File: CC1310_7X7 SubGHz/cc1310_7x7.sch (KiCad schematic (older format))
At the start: 41 parts, among them Y1 32.768kHz

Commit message: added LEDs and buttons
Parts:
- removed L15: TBD, symbol INDUCTOR
- removed L? (x2): INDUCTOR, symbol INDUCTOR
- removed R12: DNM, symbol R
- removed R13: 0, symbol R
- added C?: 15nF, symbol C
- added C?: DNM, symbol C
- added D? (x4): LED, symbol LED
- added R? (x4): 680E, symbol R
- added R?: 1K, symbol R
- added R?: R, symbol R
- added SW? (x2): SW_PUSH, symbol SW_PUSH
- L12, L21: renamed from L?; value INDUCTOR -> 7.5nH
- Y2: renamed from Y?; value Crystal -> 24MHz
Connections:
- net labels added: DIO_19, DIO_20, DIO_21, DIO_22, DIO_23, DIO_24, DIO_25, DIO_26, DIO_27, DIO_28, DIO_29, DIO_30, JTAG_TCK, JTAG_TMS, nRESET
- net labels removed: VDD
- wire segments 60 -> 140
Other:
- moved on the sheet: C11, C21, C22, C231, C351, C41, C461, C471, C51, L11, L12, L21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

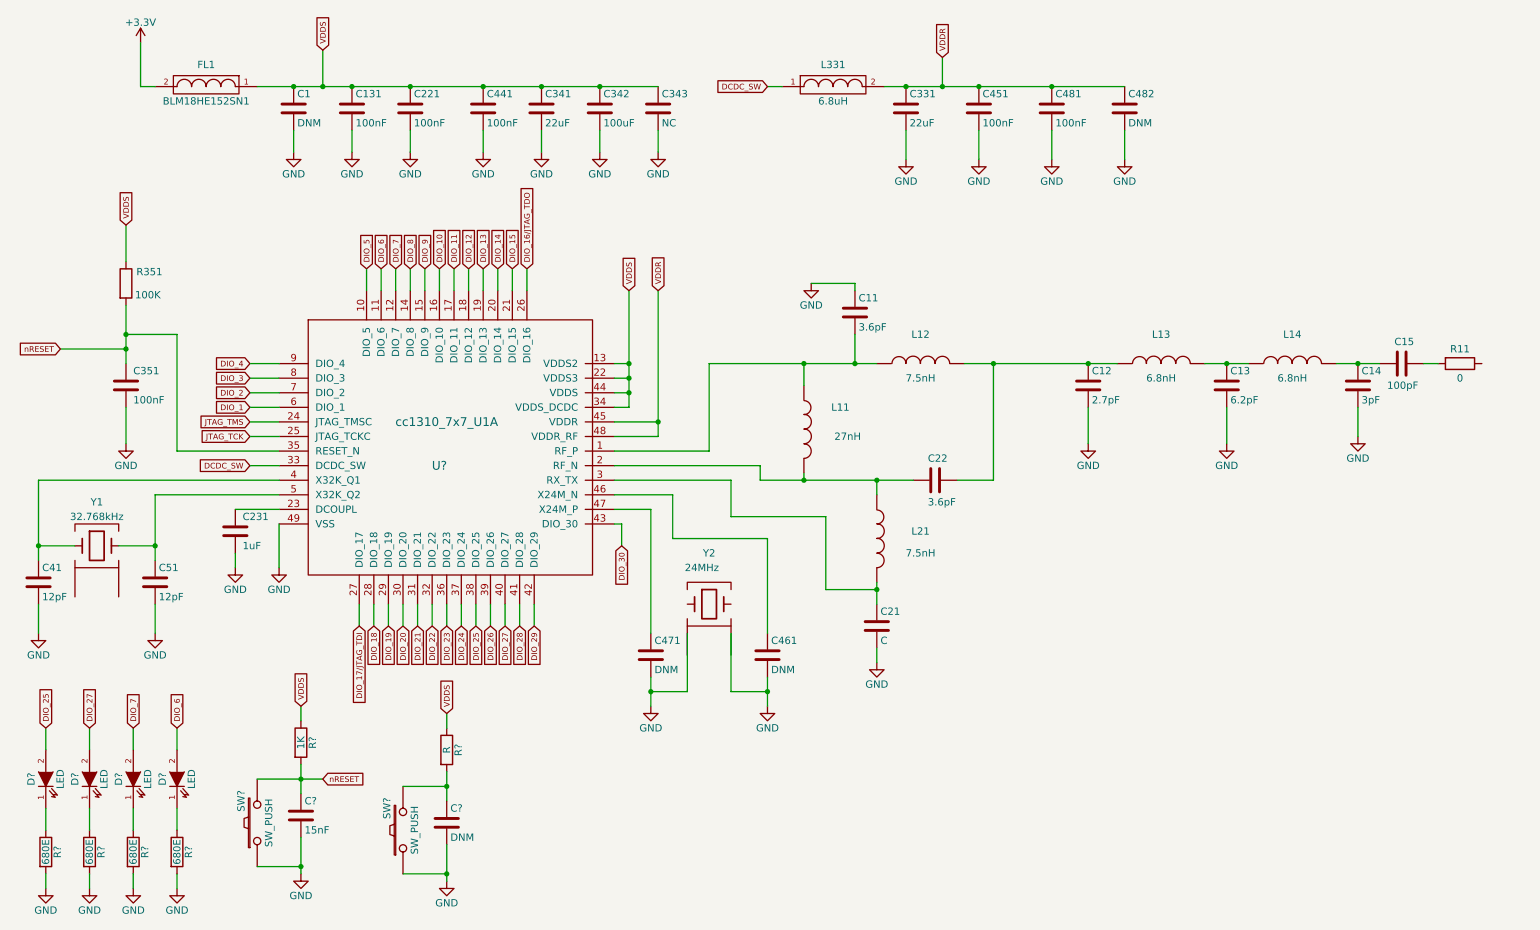
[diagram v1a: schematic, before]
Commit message: de annotated the components; added text for power section; added text for peripherals
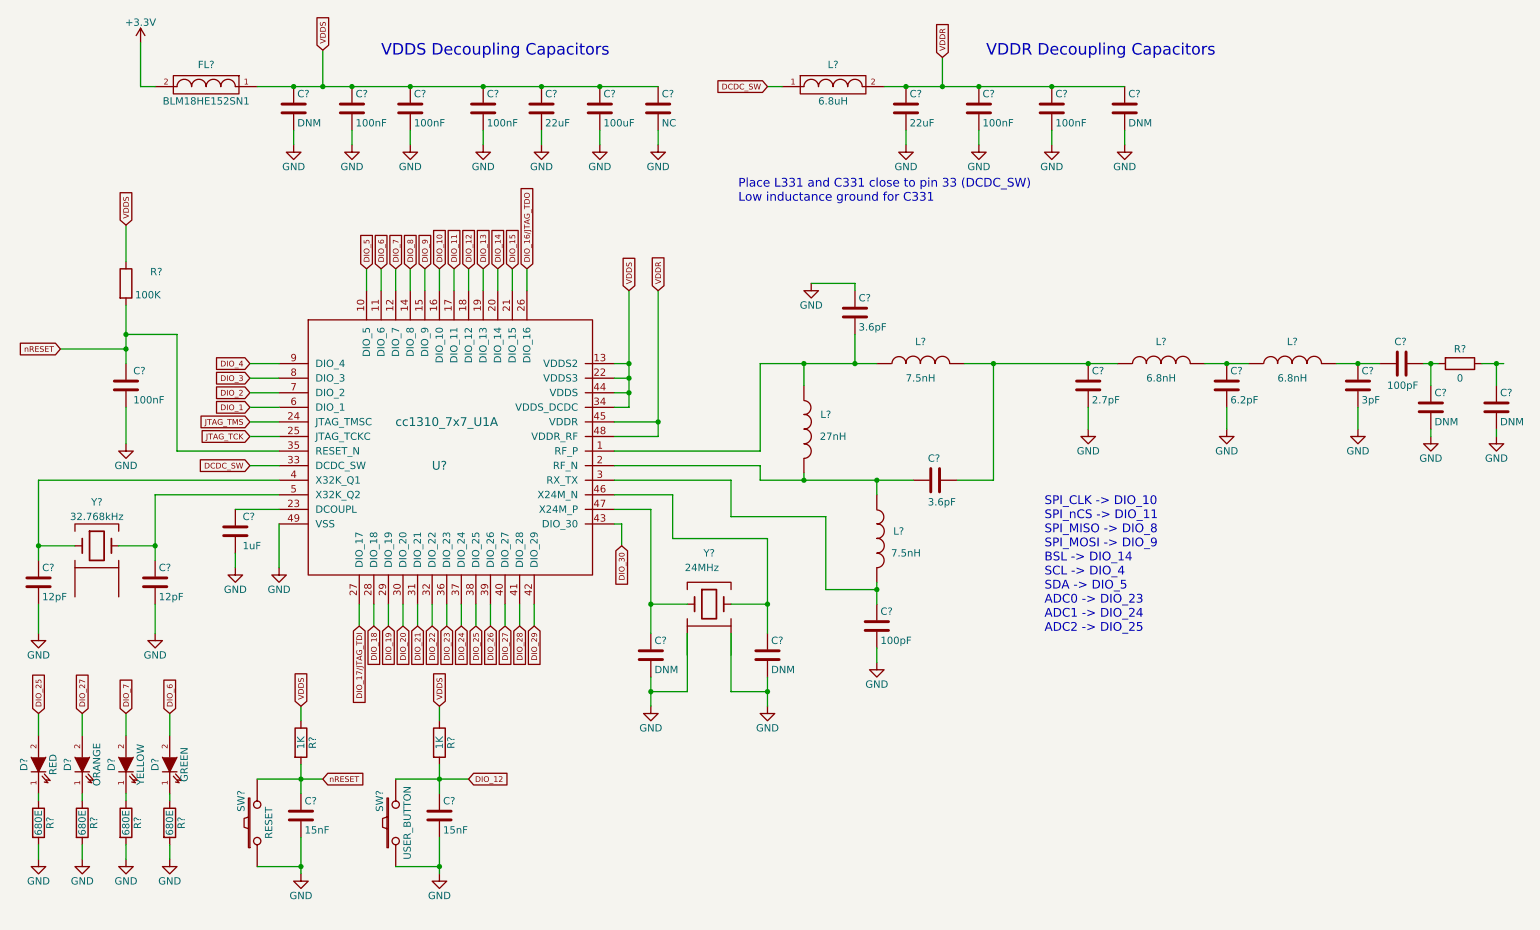
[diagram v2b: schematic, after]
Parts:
- added C? (x2): DNM, symbol C
- C?: renamed from C351; footprint (none) -> Capacitors_SMD:C_0402
- C?: renamed from C21; value C -> 100pF
- C?: value DNM -> 15nF
- D?: value LED -> RED
- D?: value LED -> ORANGE
- D?: value LED -> YELLOW
- D?: value LED -> GREEN
- R?: renamed from R351; footprint (none) -> Resistors_SMD:R_0402
- R?: value R -> 1K
- SW?: value SW_PUSH -> RESET
- SW?: value SW_PUSH -> USER_BUTTON
- renumbered C1 to C?, C131 to C?, C221 to C?, C441 to C?, C341 to C?, C342 to C?, C343 to C?, C331 to C?, C482 to C?, C451 to C?, C481 to C?, C41 to C?, C51 to C?, C231 to C?, C471 to C?, C461 to C?, C11 to C?, C22 to C?, C12 to C?, C13 to C?, C14 to C?, C15 to C?, FL1 to FL?, L331 to L?, L12 to L?, L21 to L?, L13 to L?, L14 to L?, L11 to L?, R11 to R?, Y1 to Y?, Y2 to Y?
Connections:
- net DIO_12: now also C?.1, R?.2, SW?.2
- net GND: now also C?.2, C?.2
- net at C?.1, U?.46 (X24M_N): now also Y?.2
- net at C?.1, U?.47 (X24M_P): now also Y?.1
- net at C?.1, R?.2: now also C?.1
- net at R?.1: now also C?.1
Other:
- note added: "Place L331 and C331 close to pin 33 (DCDC_SW)\nLow inductance ground for C331"
- note added: "SPI_CLK -> DIO_10\nSPI_nCS -> DIO_11\nSPI_MISO -> DIO_8\nSPI_MOSI -> DIO_9\nBSL -> DIO_14\nSCL -> DIO_4\nSDA -> DIO_5\nADC0 -> DIO_23\nADC1 -> DIO_24\nADC2 -> DIO_25"
- note added: "VDDR Decoupling Capacitors"
- note added: "VDDS Decoupling Capacitors"
- moved on the sheet: C?, D?, R?, SW?

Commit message: added XBee and JTAG pinouts
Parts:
- added R? (x2): 3.3K, Resistors_SMD:R_0402, symbol R
- added R? (x2): 0E, symbol R_Small
- added U?: XBEE, symbol XBEE
- added U?: JTAG, symbol JTAG
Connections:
- net +3V3: now also U?.1 (VCC)
- net DIO_12: no longer C?.1, R?.2, SW?.2
- net GND: now also U?.10 (GND), U?.3 (GND), U?.5 (GND), U?.9 (GND)
- net JTAG_TCK: now also U?.4 (SWDCLK/TCK)
- net JTAG_TMS: now also U?.2 (SWDIO/TMS)
- net VDDS: now also R?.2, R?.1, R?.1, U?.1 (V_REF); no longer R?.1
- net nRESET: now also R?.1, U?.10 (nRESET), U?.5 (RESET); no longer R?.2
- net DIO_1 renamed TX
- net TX: now also U?.2 (DOUT)
- net DIO_10 renamed SPI_CLK
- net SPI_CLK: now also U?.15 (AD5/DIO5)
- net DIO_11 renamed SPI_nCS
- net SPI_nCS: now also U?.12 (CTS/DIO7)
- net DIO_14 renamed BSL
- net BSL: now also C?.1, R?.2, SW?.2, U?.13 (ON/SLEEP)
- net DIO_16/JTAG_TDO renamed JTAG_TDO
- net JTAG_TDO: now also U?.6 (SWO/TDO)
- net DIO_17/JTAG_TDI renamed JTAG_TDI
- net JTAG_TDI: now also U?.8 (TDI)
- net DIO_18 renamed PWM0
- net PWM0: now also U?.6 (PWM0/RSSI)
- net DIO_19 renamed PWM1
- net PWM1: now also U?.7 (PWM1)
- net DIO_2 renamed RX
- net RX: now also U?.3 (DIN)
- net DIO_25 renamed RED_LED
- net DIO_26 renamed AD3
- net AD3: now also U?.11 (AD4/DIO4)
- net DIO_27 renamed ORANGE_LED
- net DIO_28 renamed AD2
- net AD2: now also U?.16 (RTS/AD6/DIO6)
- net DIO_29 renamed AD1
- net AD1: now also U?.17 (AD3/DIO3)
- net DIO_30 renamed AD0
- net AD0: now also U?.18 (AD2/DIO2)
- net DIO_4 renamed SCL
- net SCL: now also R?.2, U?.19 (AD1/DIO1)
- net DIO_5 renamed SDA
- net SDA: now also R?.2, U?.20 (AD0/DIO0)
- net DIO_6 renamed GREEN_LED
- net DIO_7 renamed YELLOW_LED
- net DIO_8 renamed SPI_MISO
- net SPI_MISO: now also U?.9 (DTR/DI8)
- net DIO_9 renamed SPI_MOSI
- net SPI_MOSI: now also U?.4 (DO8)
- new net: R?.2, U?.14 (VREF)
- new net: R?.1, U?.8 (RESERVED)
- new net DIO_xx: R?.1, R?.2
- no-connect marks 0 -> 1
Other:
- note removed: "SPI_CLK -> DIO_10\nSPI_nCS -> DIO_11\nSPI_MISO -> DIO_8\nSPI_MOSI -> DIO_9\nBSL -> DIO_14\nSCL -> DIO_4\nSDA -> DIO_5\nADC0 -> DIO_23\nADC1 -> DIO_24\nADC2 -> DIO_25"
- moved on the sheet: C?, R?

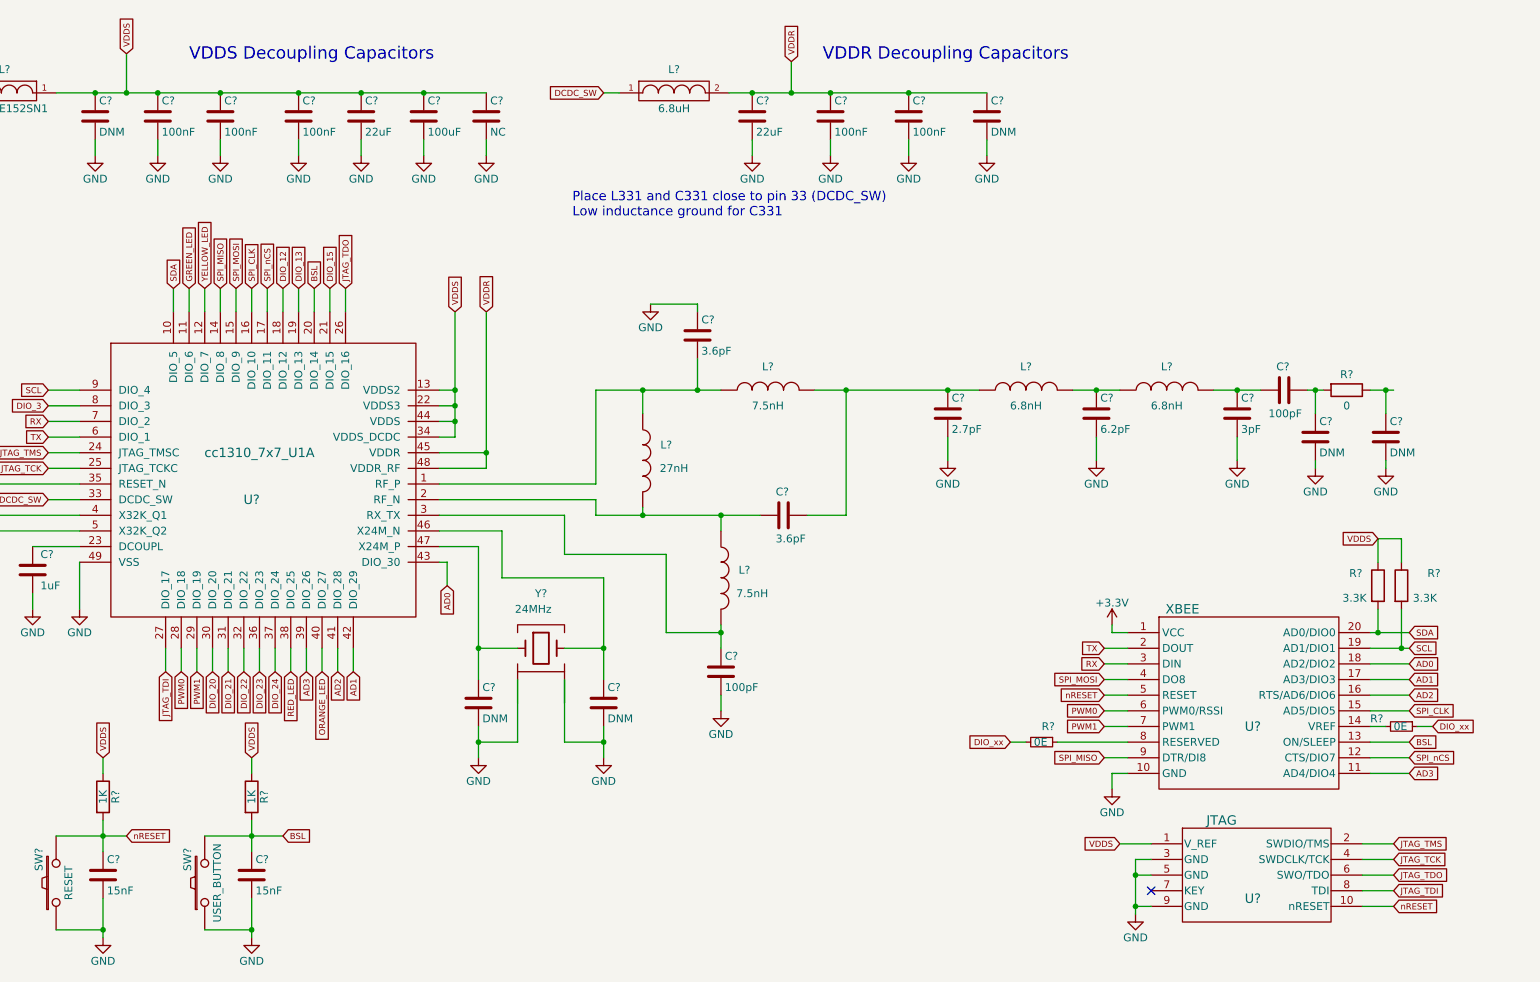
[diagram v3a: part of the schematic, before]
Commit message: modified schematic; added si7006, ltr303 library
modified schematic to XBee specs like openmote
added Si7006 library part
added LTR303-ALS library part
edited 24MHz cryatal library
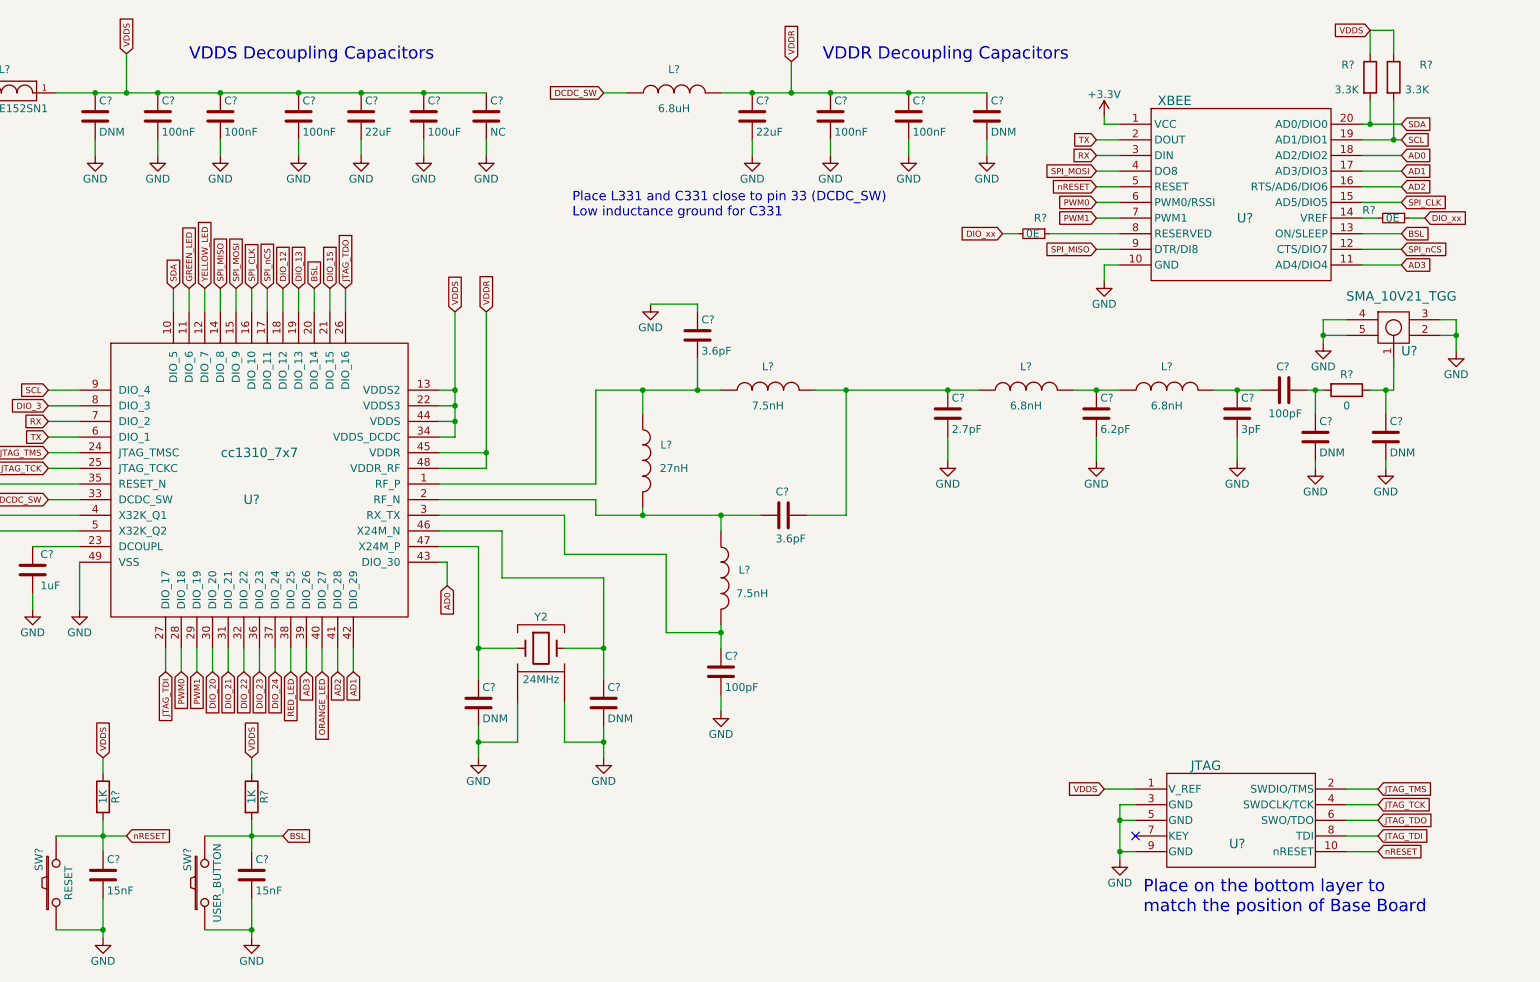
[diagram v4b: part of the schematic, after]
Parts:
- removed L?: 6.8uH, symbol FILTER
- removed U?: cc1310_7x7_U1A, symbol cc1310_7x7_U1A
- removed Y?: 24MHz, symbol Crystal
- added L?: 6.8uH, symbol INDUCTOR
- added U?: cc1310_7x7, symbol cc1310_7x7
- added U?: SMA_10V21_TGG, symbol SMA_10V21_TGG
- added Y2: 24MHz, symbol Crystal
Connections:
- net AD0: now also U?.43 (DIO_30)
- net AD1: now also U?.42 (DIO_29)
- net AD2: now also U?.41 (DIO_28)
- net AD3: now also U?.39 (DIO_26)
- net BSL: now also U?.20 (DIO_14)
- net DCDC_SW: now also L?.1, U?.33 (DCDC_SW)
- net DIO_12: now also U?.18 (DIO_12)
- net DIO_13: now also U?.19 (DIO_13)
- net DIO_15: now also U?.21 (DIO_15)
- net DIO_20: now also U?.30 (DIO_20)
- net DIO_21: now also U?.31 (DIO_21)
- net DIO_22: now also U?.32 (DIO_22)
- net DIO_23: now also U?.36 (DIO_23)
- net DIO_24: now also U?.37 (DIO_24)
- net DIO_3: now also U?.8 (DIO_3)
- net GND: now also U?.2, U?.3, U?.4, U?.49 (VSS), U?.5, Y2.~
- net GREEN_LED: now also U?.11 (DIO_6)
- net JTAG_TCK: now also U?.25 (JTAG_TCKC)
- net JTAG_TDI: now also U?.27 (DIO_17)
- net JTAG_TDO: now also U?.26 (DIO_16)
- net JTAG_TMS: now also U?.24 (JTAG_TMSC)
- net ORANGE_LED: now also U?.40 (DIO_27)
- net PWM0: now also U?.28 (DIO_18)
- net PWM1: now also U?.29 (DIO_19)
- net RED_LED: now also U?.38 (DIO_25)
- net RX: now also U?.7 (DIO_2)
- net SCL: now also U?.9 (DIO_4)
- net SDA: now also U?.10 (DIO_5)
- net SPI_CLK: now also U?.16 (DIO_10)
- net SPI_MISO: now also U?.14 (DIO_8)
- net SPI_MOSI: now also U?.15 (DIO_9)
- net SPI_nCS: now also U?.17 (DIO_11)
- net TX: now also U?.6 (DIO_1)
- net VDDR: now also L?.2, U?.45 (VDDR), U?.48 (VDDR_RF)
- net VDDS: now also U?.13 (VDDS2), U?.22 (VDDS3), U?.34 (VDDS_DCDC), U?.44 (VDDS)
- net YELLOW_LED: now also U?.12 (DIO_7)
- net nRESET: now also U?.35 (RESET_N)
- net at C?.1, Y?.1: now also U?.4 (X32K_Q1)
- net at C?.1, Y?.2: now also U?.5 (X32K_Q2)
- net at C?.1: now also U?.23 (DCOUPL)
- net at C?.2, L?.1, L?.1: now also U?.1 (RF_P)
- net at C?.2, L?.1, L?.2: now also U?.2 (RF_N)
- net at C?.1, L?.2: now also U?.3 (RX_TX)
- net at C?.1: now also U?.46 (X24M_N), Y2.2
- net at C?.1: now also U?.47 (X24M_P), Y2.1
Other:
- note added: "Place on the bottom layer to \nmatch the position of Base Board"
- moved on the sheet: R?, U?
